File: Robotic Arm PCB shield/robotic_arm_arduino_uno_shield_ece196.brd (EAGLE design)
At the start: 53.3 x 53.3 mm, 37 parts, among them J1 (ID,OD)=(2.1,5.5)MM

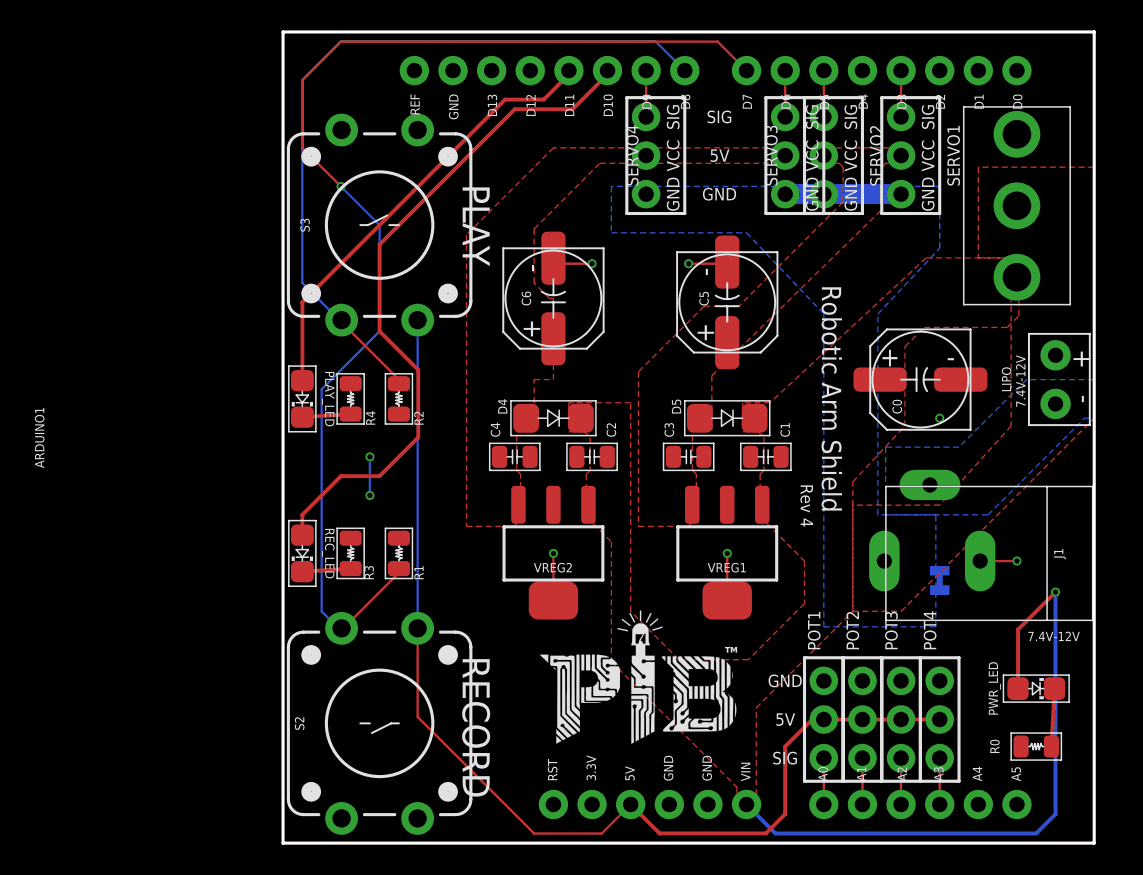
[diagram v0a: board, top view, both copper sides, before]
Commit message: Rev 5:  Add 1000uF capacitors for potential performance boost by reducing any ripple.  Add tons of vias by voltage regulators to help with heat dissipation.  Update all components to newest libraries.
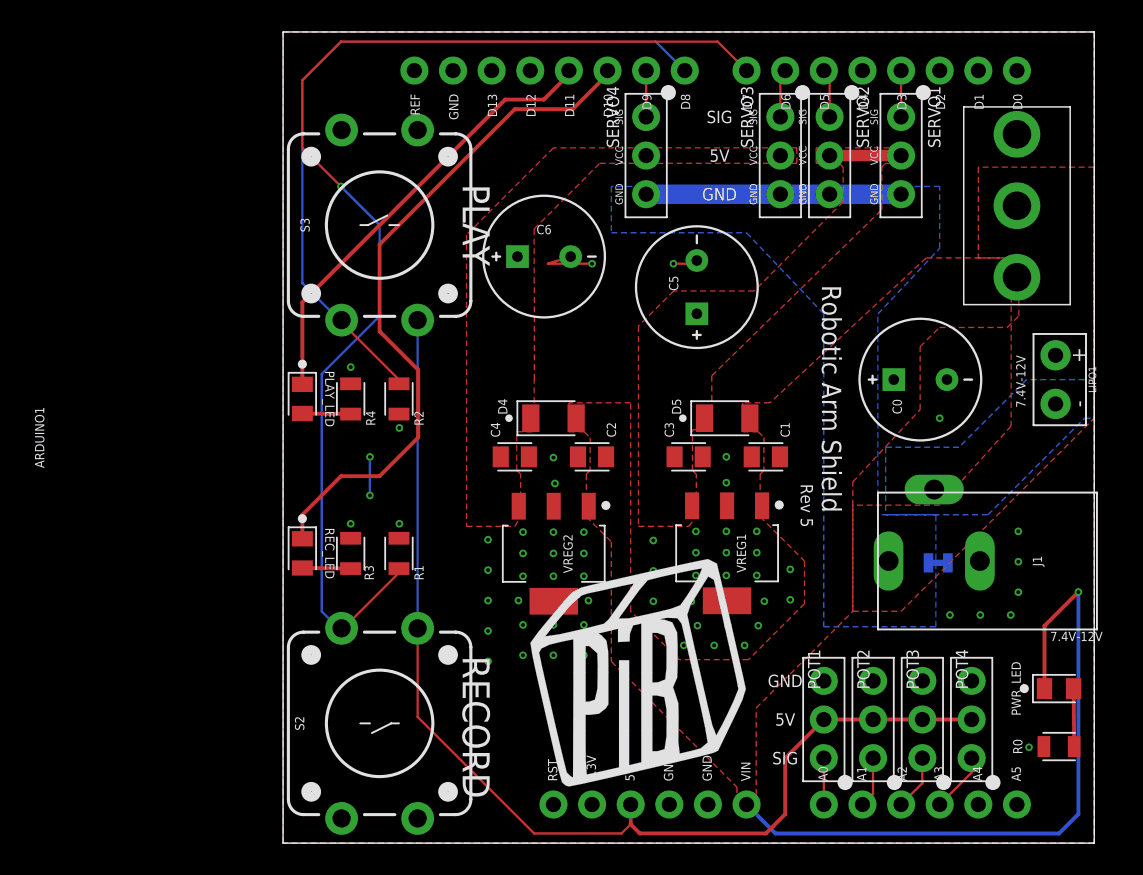
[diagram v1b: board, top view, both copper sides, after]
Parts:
- removed U$1: (no value), PiB_logo:PIB-LOGO
- added U$4: (no value), PiB_logo:PIB_LOGO_5MM
- C0: value 220uF/16V -> 1000uF/16V; device PiB_capacitors:_AE_SMD_L6.6-W6.6 -> PiB_capacitors:_AE_PTH_DIA8-LS3.5-H21.50
- C1, C2: value 0.22uF/50V -> 0.1uF/35V; device PiB_capacitors:_CER_SMD-805 -> PiB_capacitors:CAPC2012X95_SMD-0805
- C3, C4: value 0.1uF/50V -> 0.1uF/35V; device PiB_capacitors:_CER_SMD-805 -> PiB_capacitors:CAPC2012X95_SMD-0805
- C5, C6: value 100UF/16V -> 1000uF/16V; device PiB_capacitors:_AE_SMD_L6.6-W6.6 -> PiB_capacitors:_AE_PTH_DIA8-LS3.5-H21.50
- D4, D5: device PiB_discrete_semiconductors:SOD123F -> PiB_discrete_semiconductors:SODFL3516X170
- J1: value (ID,OD)=(2.1,5.5)MM -> 5A/28V
- LIPO1: value 7.4V -> BATTERY_LIPO_2S
- PLAY_LED, PWR_LED, REC_LED: device PiB_leds:LED_SMD-805_ -> PiB_leds:LEDC2012X120_LED-0805
- POT1, POT2, POT3, POT4: value 10KΩ -> 10K; device PiB_resistors:CONNECTOR_POTENTIOMETER_NO-MARKINGS_FEMALE-HEADER -> PiB_resistors:HDRVR3W64P254_1X3_812X254X850B
- R0, R1, R2: value 10KΩ -> 10K; device PiB_resistors:RESISTOR_SMD-805 -> PiB_resistors:RESC2012X60_SMD-0805
- R3, R4: value 1KΩ -> 1K; device PiB_resistors:RESISTOR_SMD-805 -> PiB_resistors:RESC2012X60_SMD-0805
- SERVO1, SERVO2, SERVO3, SERVO4: device PiB:CONNECTOR_SERVO -> PiB_motors:HDRVR3W64P254_1X3_812X254X850B
- SUPPLY14: value 2PT_GND_TIE -> NET_BRIDGE; device PiB_power_symbols:2PT_GND_TIE -> PiB_power_symbols:NET_BRIDGE
- U$3: device PiB_logo:PIB-LOGO -> PiB_logo:PIB_LOGO_5MM
- VREG1, VREG2: value LM340MP-5 1.5A/5V -> MIC39100-5.0 5V/1A; device PiB_ic_power:SOT223-4 -> PiB_ic_power:SOT229P700X180-4
- moved U$3 18.0 mm to (5.80, 25.0), flipped to the bottom, turned to 270 degrees
- moved POT4 3.30 mm to (38.9, 5.59)
- moved SERVO3 3.00 mm to (26.4, 47.8)
- moved J1 2.94 mm to (36.5, 18.6)
- moved POT3 2.90 mm to (35.7, 5.59)
- moved SERVO1 2.84 mm to (34.3, 47.8)
- moved SERVO4 2.84 mm to (17.5, 47.8)
- moved C6 2.82 mm to (10.8, 38.6), turned to 0 degrees
- moved SERVO2 2.69 mm to (29.6, 47.8)
- moved POT2 2.63 mm to (32.5, 5.59)
- moved POT1 2.54 mm to (29.2, 5.59)
- moved C5 2.24 mm to (20.9, 36.6)
- moved PWR_LED 1.50 mm to (44.7, 10.2)
- moved R0 1.50 mm to (44.7, 6.35)
- moved SUPPLY14 1.16 mm to (36.7, 18.4), turned to 180 degrees
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- renumbered LIPO to LIPO1
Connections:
- net +: now also S1.P; no longer S1.2
- net -: now also J1.GND_BATTERY; no longer J1.GND@2
- net D3: now also SERVO1.SIG; no longer SERVO1.1
- net D5: now also SERVO2.SIG; no longer SERVO2.1
- net D6: now also SERVO3.SIG; no longer SERVO3.1
- net D9: now also SERVO4.SIG; no longer SERVO4.1
- net GND: now also C0.-, C5.-, C6.-, J1.GND_JACK; no longer C0.K, C5.K, C6.K, J1.GND@1
- net NGND: now also SERVO1.GND, SERVO2.GND, SERVO3.GND, SERVO4.GND; no longer SERVO1.3, SERVO2.3, SERVO3.3, SERVO4.3
- net VCC_1: now also C5.+, SERVO1.VCC, SERVO2.VCC; no longer C5.A, SERVO1.2, SERVO2.2
- net VCC_2: now also C6.+, SERVO3.VCC, SERVO4.VCC; no longer C6.A, SERVO3.2, SERVO4.2
- net VIN: now also C0.+, S1.S1; no longer C0.A, S1.1
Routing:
- net GND: track 17.3 -> 8.74 mm, vias 8 -> 64
- net VCC_1: track 0.00 -> 4.70 mm
- net 5V: track 71.1 -> 72.8 mm
- net NGND: track 15.2 -> 16.8 mm
- net VIN: track 43.6 -> 45.0 mm
- net A3: track 3.05 -> 3.92 mm
- net D8: track 50.5 -> 49.7 mm
- net A2: track 3.05 -> 3.63 mm
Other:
- board text added: "Rev 5"
- board text added: "Rev 5 Designed by: Buu Truong CADed by: MrSwirlyEyes"
- board text removed: "Rev 4"
- board text removed: "Rev 4 Designed by: Buu Truong CADed by: MrSwirlyEyes"
